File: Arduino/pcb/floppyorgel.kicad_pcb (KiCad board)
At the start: 2 copper layers, 50 x 50 mm, 56 parts, among them J1 VCC_Power_Select, J2 Floppy-Bus, J3 MAX485 Socket, J4 Floppy-Bus, J5 Buck-Converter-5V, J6 Buck-Converter-12V, J7 Floppy-Power, J8 IBM_PC_Floppy_IDC, J9 FTDI, Q1 IRLML2060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

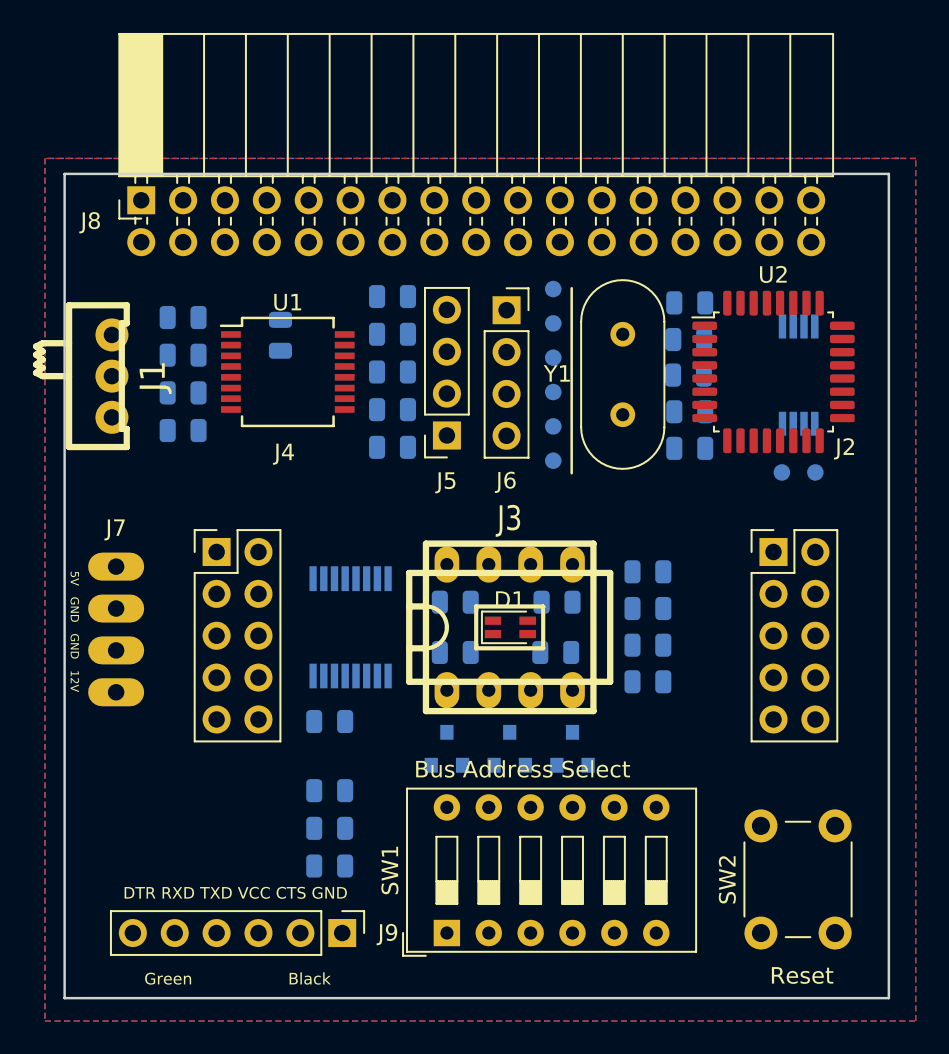
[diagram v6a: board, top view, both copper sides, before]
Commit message: pcb: cut floppy edge + beautification
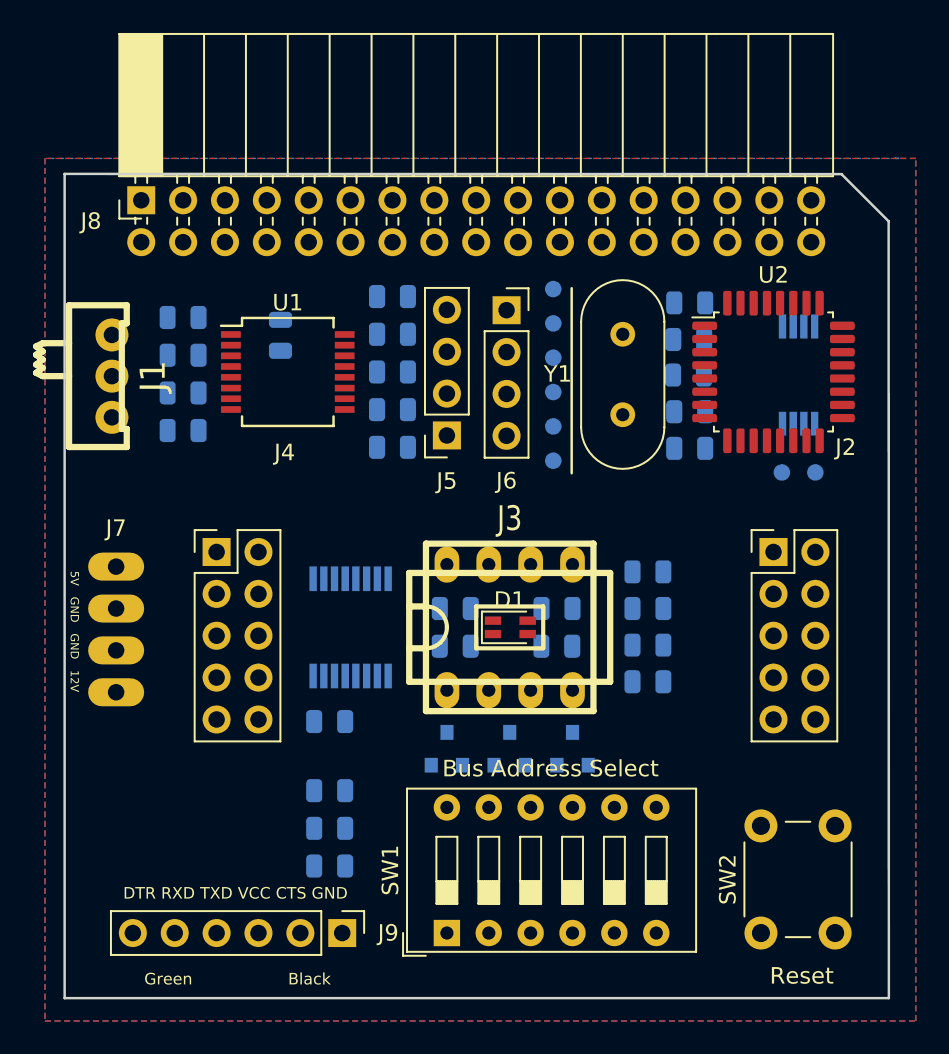
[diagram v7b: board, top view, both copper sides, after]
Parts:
- moved L1 0.63 mm to (107.6, 138.9)
- moved R15 0.39 mm to (129.9, 128.7)
- moved C1 0.38 mm to (123.7, 126.4)
- moved R14 0.38 mm to (123.7, 128.7)
- moved R16 0.38 mm to (129.9, 126.4)
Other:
- outline, holes or cut-outs redrawn
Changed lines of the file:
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@@
   (general
     (thickness 1.6)
-    (drawings 19)
+    (drawings 20)
     (tracks 0)
     (zones 0)
@@
   )
   (module Capacitor_SMD:C_0805_2012Metric (layer B.Cu)
-    (at 123.698 125.984)
+    (at 123.698 126.365)
     (descr "Capacitor SMD 0805 (2012 Metric), square (rectangular) end terminal, IPC_7351 nominal, (Body size source: https://docs.google.com/spreadsheets/d/1BsfQQcO9C6DZCsRaXUlFlo91Tg2WpOkGARC1WS5S8t0/edit?usp=sharing), generated with kicad-footprint-generator")
     (tags capacitor)
@@
   )
   (module Resistor_SMD:R_0805_2012Metric (layer B.Cu)
-    (at 123.698 129.032 180)
+    (at 123.698 128.651 180)
     (descr "Resistor SMD 0805 (2012 Metric), square (rectangular) end terminal, IPC_7351 nominal, (Body size source: https://docs.google.com/spreadsheets/d/1BsfQQcO9C6DZCsRaXUlFlo91Tg2WpOkGARC1WS5S8t0/edit?usp=sharing), generated with kicad-footprint-generator")
     (tags resistor)
@@
   )
   (module Resistor_SMD:R_0805_2012Metric (layer B.Cu)
-    (at 129.794 129.032)
+    (at 129.8575 128.651)
     (descr "Resistor SMD 0805 (2012 Metric), square (rectangular) end terminal, IPC_7351 nominal, (Body size source: https://docs.google.com/spreadsheets/d/1BsfQQcO9C6DZCsRaXUlFlo91Tg2WpOkGARC1WS5S8t0/edit?usp=sharing), generated with kicad-footprint-generator")
     (tags resistor)
@@
   )
   (module Resistor_SMD:R_0805_2012Metric (layer B.Cu)
-    (at 129.8725 125.984 180)
+    (at 129.8725 126.365 180)
     (descr "Resistor SMD 0805 (2012 Metric), square (rectangular) end terminal, IPC_7351 nominal, (Body size source: https://docs.google.com/spreadsheets/d/1BsfQQcO9C6DZCsRaXUlFlo91Tg2WpOkGARC1WS5S8t0/edit?usp=sharing), generated with kicad-footprint-generator")
     (tags resistor)
@@
   )
   (module logo:logo (layer B.Cu)
-    (at 108.204 138.938 180)
+    (at 107.569 138.938 180)
     (fp_text reference L1 (at 0 0) (layer B.SilkS) hide
       (effects (font (size 1.524 1.524) (thickness 0.3)) (justify mirror))
@@
     )
   )
+  (gr_line (start 149.987 102.87) (end 147.1295 100.0125) (layer Edge.Cuts) (width 0.15))
   (gr_text "Green                   Black" (at 110.49 148.844) (layer F.SilkS)
     (effects (font (size 0.7 0.7) (thickness 0.15)))
@@
     (effects (font (size 1 1) (thickness 0.15)))
   )
-  (gr_text "Bus Address Select" (at 127.762 136.144) (layer F.SilkS)
+  (gr_text "Bus Address Select" (at 129.4765 136.0805) (layer F.SilkS)
     (effects (font (size 1 1) (thickness 0.15)))
   )
@@
   (gr_line (start 100 150) (end 100 100) (angle 90) (layer Edge.Cuts) (width 0.15))
   (gr_line (start 150 150) (end 100 150) (angle 90) (layer Edge.Cuts) (width 0.15))
-  (gr_line (start 150 100) (end 150 150) (angle 90) (layer Edge.Cuts) (width 0.15))
-  (gr_line (start 100 100) (end 150 100) (angle 90) (layer Edge.Cuts) (width 0.15))
-  (zone (net 3) (net_name GND) (layer F.Cu) (hatch edge 0.508)
-    (connect_pads (clearance 0.508))
-    (min_thickness 0.254)
-    (fill yes (arc_segments 32) (thermal_gap 0.508) (thermal_bridge_width 0.508))
-    (polygon
-      (pts
-        (xy 151.638 99.06) (xy 98.806 99.06) (xy 98.806 151.384) (xy 151.638 151.384)
-      )
-    )
-  )
+  (gr_line (start 149.987 102.87) (end 150 150) (angle 90) (layer Edge.Cuts) (width 0.15))
+  (gr_line (start 100 100) (end 147.1295 100.0125) (angle 90) (layer Edge.Cuts) (width 0.15))
   (zone (net 3) (net_name GND) (layer B.Cu) (hatch edge 0.508)
     (connect_pads (clearance 0.508))
@@
       )
     )
+  )
+  (zone (net 3) (net_name GND) (layer F.Cu) (hatch edge 0.508)
+    (connect_pads (clearance 0.508))
+    (min_thickness 0.254)
+    (fill yes (arc_segments 32) (thermal_gap 0.508) (thermal_bridge_width 0.508))
+    (polygon
+      (pts
+        (xy 151.638 99.06) (xy 98.806 99.06) (xy 98.806 151.384) (xy 151.638 151.384)
+      )
+    )

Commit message: pcb: some routing
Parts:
- turned C7 to 0 degrees
- turned R1 to 180 degrees
- turned R16 to 0 degrees
- turned R5 to 0 degrees
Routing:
- net Net-(J9-Pad5): track 0.00 -> 234.9 mm, vias 0 -> 6
- net GND: track 0.00 -> 222.9 mm, vias 0 -> 10
- net Net-(C3-Pad2): track 0.00 -> 104.0 mm, vias 0 -> 4
- net VCC: track 0.00 -> 95.4 mm, vias 0 -> 8
- net Net-(J9-Pad4): track 0.00 -> 86.5 mm, vias 0 -> 6
- net /MCU/RESET: track 0.00 -> 77.0 mm, vias 0 -> 14
- net /Led/LATCH_LED: track 0.00 -> 72.9 mm, vias 0 -> 7
- net /Floppy/LATCH_ADDR: track 0.00 -> 64.4 mm, vias 0 -> 7
- net /Bus/BUS_POWER: track 0.00 -> 54.2 mm, vias 0 -> 2
- net /5V_ISP: track 0.00 -> 52.4 mm, vias 0 -> 2
- net /Floppy/SCK: track 0.00 -> 49.8 mm, vias 0 -> 5
- net /Floppy/MISO: track 0.00 -> 46.0 mm, vias 0 -> 3
- net /Floppy/12V_BUS: track 0.00 -> 42.8 mm, vias 0 -> 2
- net /Floppy/TRK00: track 0.00 -> 38.1 mm, vias 0 -> 3
- net /Floppy/DRIVE_SELECT: track 0.00 -> 37.1 mm, vias 0 -> 3
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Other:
- net class Default: clearance 0.2 -> 0.1; trace_width 0.25 -> 0.1; via_dia 0.6 -> 0.45; via_drill 0.4 -> 0.3
- rule pad_to_mask_clearance: 0.2 -> 0.1
- rule solder_mask_min_width: 0.25 -> 0.1
- rule trace_clearance: 0.2 -> 0.1
- rule trace_min: 0.2 -> 0.1
- rule via_min_drill: 0.3 -> 0.2
- rule via_min_size: 0.4 -> 0.45
